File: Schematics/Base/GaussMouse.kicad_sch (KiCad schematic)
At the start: 15 parts, among them J1 USB_C_Receptacle, SW1 SW_SPST, SW2 SW_SPST, U1 BNO085, U2 ESP32-S3-WROOM-1, U3 TLV1117-33

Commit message: Sensor Board Ready for Traces
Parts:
- removed U1: BNO085, LGA28_5.2X3.8_CEV, symbol GaussMouse:BNO085
- RN1: value R_Pack04 -> 5.1k
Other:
- moved on the sheet: C5, C6, C7, R1, SW1, SW2, U2

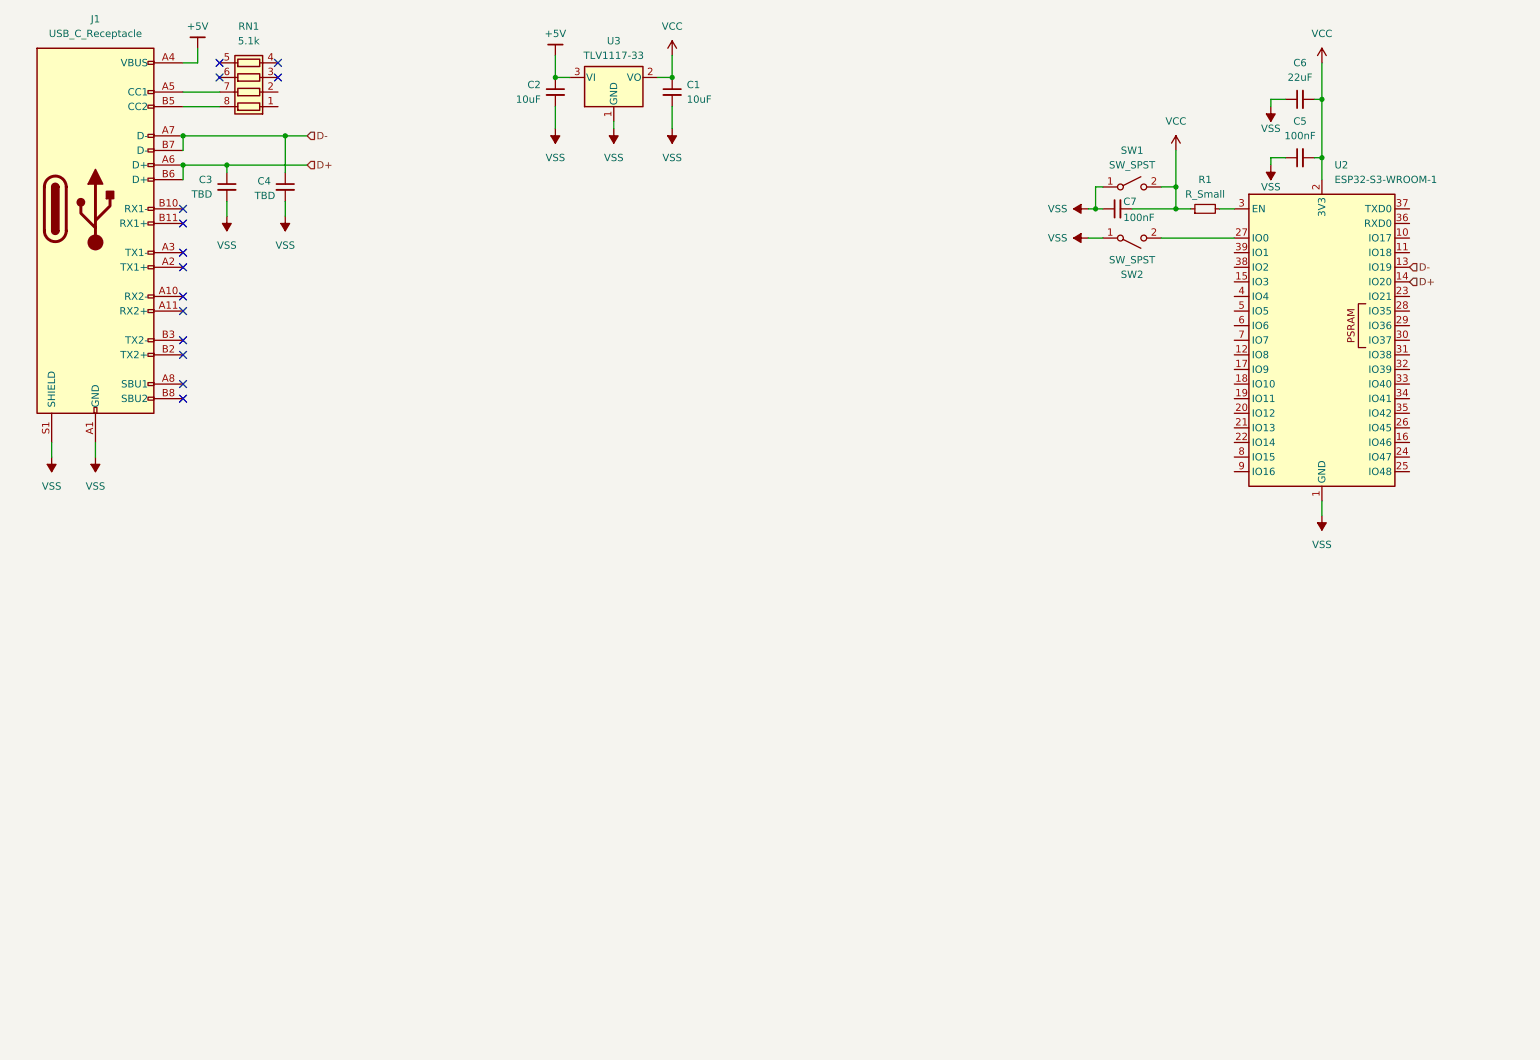
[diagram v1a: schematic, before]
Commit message: Commit for backup. Short on sensor board so I'm going to redo it
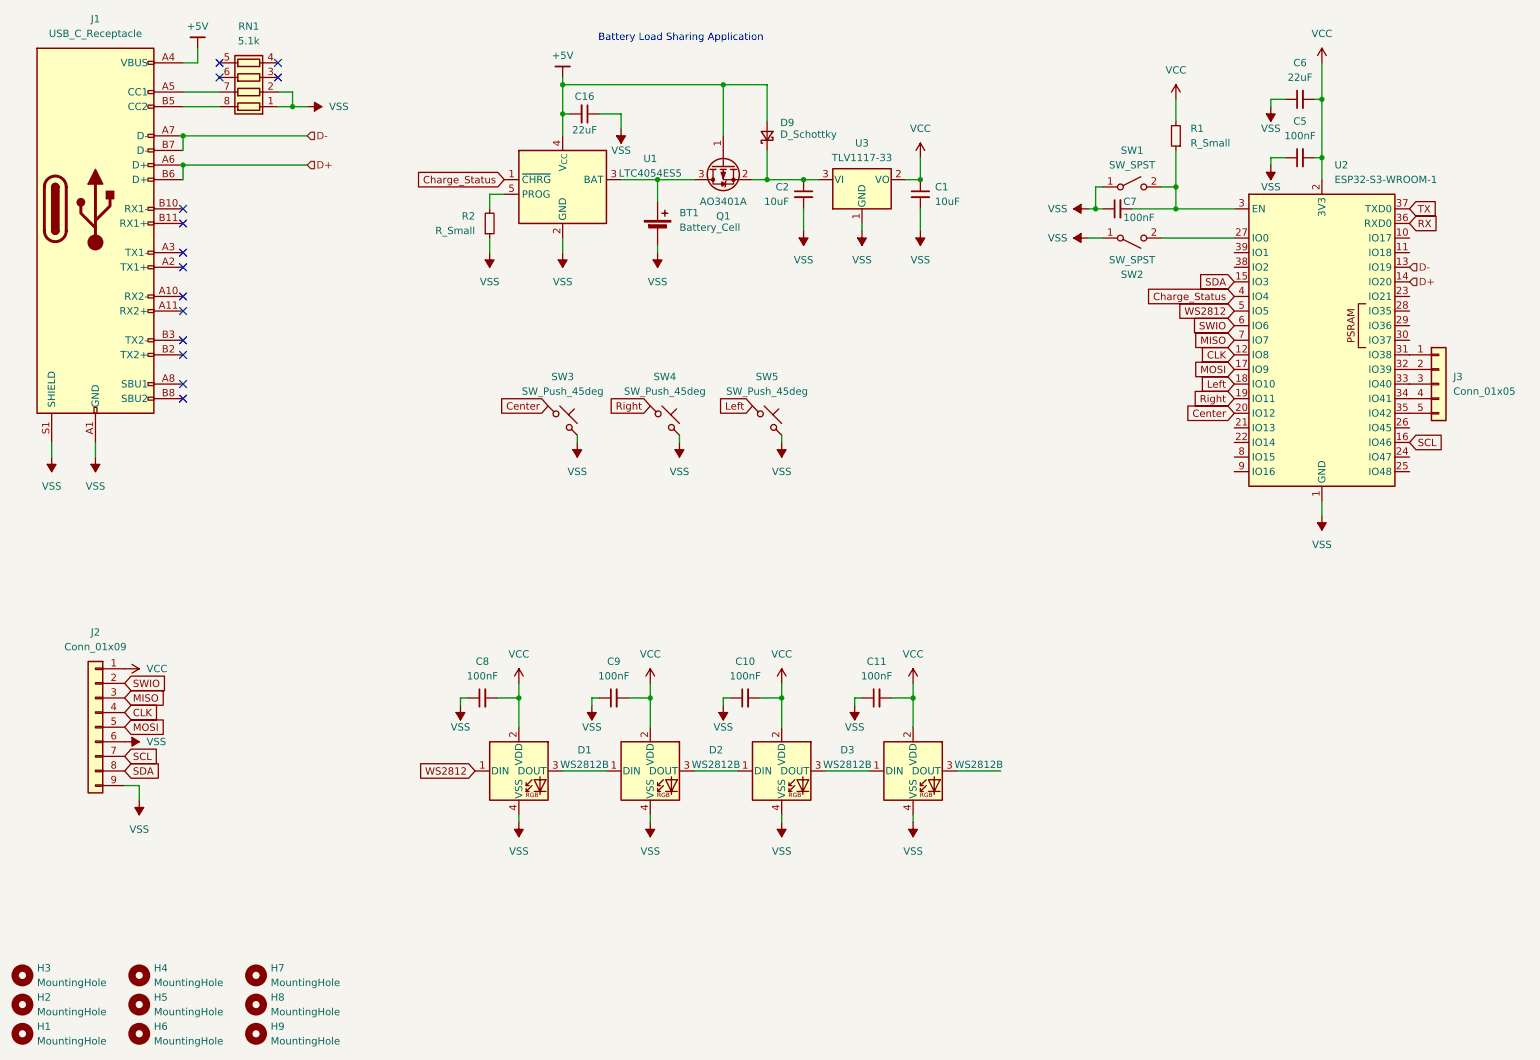
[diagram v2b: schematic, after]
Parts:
- removed C3, C4: TBD, symbol Device:C_Small
- added BT1: Battery_Cell, Connector_PinHeader_2.54mm:PinHeader_1x02_P2.54mm_Vertical, symbol Device:Battery_Cell
- added C10, C11, C8, C9: 100nF, Capacitor_SMD:C_0805_2012Metric, symbol Device:C_Small
- added C16: 22uF, Capacitor_SMD:C_0805_2012Metric, symbol Device:C_Small
- added D1, D2, D3, D4: WS2812B, UL_LED:SK6812SIDE-A-RVS, symbol LED:WS2812B
- added D9: D_Schottky, Diode_SMD:D_SOD-123, symbol Device:D_Schottky_Small
- added H1, H2, H3, H4, H5, H6, H7, H8, H9: MountingHole, UL_Standoff:M2ThreadedStandoff, symbol Mechanical:MountingHole
- added J2: Conn_01x09, GaussMouse:CON_526100933_MOL, symbol Connector_Generic:Conn_01x09
- added J3: Conn_01x05, Connector_PinHeader_2.54mm:PinHeader_1x05_P2.54mm_Vertical, symbol Connector_Generic:Conn_01x05
- added Q1: AO3401A, Package_TO_SOT_SMD:SOT-23, symbol Transistor_FET:AO3401A
- added R2: R_Small, Resistor_SMD:R_0805_2012Metric, symbol Device:R_Small
- added SW3, SW4, SW5: SW_Push_45deg, UL_Buttons:TS3315A, symbol Switch:SW_Push_45deg
- added U1: LTC4054ES5, Package_TO_SOT_SMD:TSOT-23-5, symbol Battery_Management:LTC4054ES5-4.2
- C1, C2, C5, C6, C7: footprint (none) -> Capacitor_SMD:C_0805_2012Metric
- R1: footprint (none) -> Resistor_SMD:R_0805_2012Metric
- RN1: footprint (none) -> Resistor_SMD:R_Array_Concave_4x0603
- SW1, SW2: footprint (none) -> UL_Buttons:TS3315A
- U3: footprint (none) -> Package_TO_SOT_SMD:SOT-223-3_TabPin2
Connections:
- net +5V: now also C16.2, D9.2 (A), Q1.1 (G), U1.4 (V_{CC}); no longer C2.1, U3.3 (VI)
- net VCC: now also R1.2, C10.2, C11.2, C8.2, C9.2, D1.2 (VDD), D2.2 (VDD), D3.2 (VDD), D4.2 (VDD), J2.1 (Pin_1); no longer C7.2, R1.1, SW1.2 (B)
- net VSS: now also RN1.1 (R1.1), RN1.2 (R2.1), BT1.2 (-), C10.1, C11.1, C16.1, C8.1, C9.1, D1.4 (VSS), D2.4 (VSS), D3.4 (VSS), D4.4 (VSS), J2.6 (Pin_6), J2.9 (Pin_9), R2.1, SW3.2, SW4.2, SW5.2, U1.2 (GND)
- net at U2.3 (EN): now also C7.2, R1.1, SW1.2 (B); no longer R1.2
- net CLK: now reaches U2.12 (IO8)
- net CLK: now also J2.4 (Pin_4)
- net SDA: now reaches U2.15 (IO3)
- net SDA: now also J2.8 (Pin_8)
- net SCL: now reaches U2.16 (IO46)
- net SCL: now also J2.7 (Pin_7)
- net MOSI: now reaches U2.17 (IO9)
- net MOSI: now also J2.5 (Pin_5)
- net Left: now reaches U2.18 (IO10)
- net Left: now also SW5.1
- net Right: now reaches U2.19 (IO11)
- net Right: now also SW4.1
- net Center: now reaches U2.20 (IO12)
- net Center: now also SW3.1
- net at U2.31 (IO38): now also J3.1 (Pin_1)
- net at U2.32 (IO39): now also J3.2 (Pin_2)
- net at U2.33 (IO40): now also J3.3 (Pin_3)
- net at U2.34 (IO41): now also J3.4 (Pin_4)
- net at U2.35 (IO42): now also J3.5 (Pin_5)
- net RX: now reaches U2.36 (RXD0)
- net TX: now reaches U2.37 (TXD0)
- net Charge_Status: now reaches U2.4 (IO4)
- net Charge_Status: now also U1.1 (~{CHRG})
- net WS2812: now reaches U2.5 (IO5)
- net WS2812: now also D1.1 (DIN)
- net SWIO: now reaches U2.6 (IO6)
- net SWIO: now also J2.2 (Pin_2)
- net MISO: now reaches U2.7 (IO7)
- net MISO: now also J2.3 (Pin_3)
- new net: C2.1, D9.1 (K), Q1.2 (S), U3.3 (VI)
- new net: D3.3 (DOUT), D4.1 (DIN)
- new net: BT1.1 (+), Q1.3 (D), U1.3 (BAT)
- new net: R2.2, U1.5 (PROG)
- new net: D1.3 (DOUT), D2.1 (DIN)
- new net: D2.3 (DOUT), D3.1 (DIN)
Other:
- note added: "Battery Load Sharing Application"
- moved on the sheet: C1, C2, R1, U3
